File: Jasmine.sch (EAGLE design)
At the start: 26 parts, among them J4 GND, J6 Vcc, U1 ESP-12F, U3 XC6206

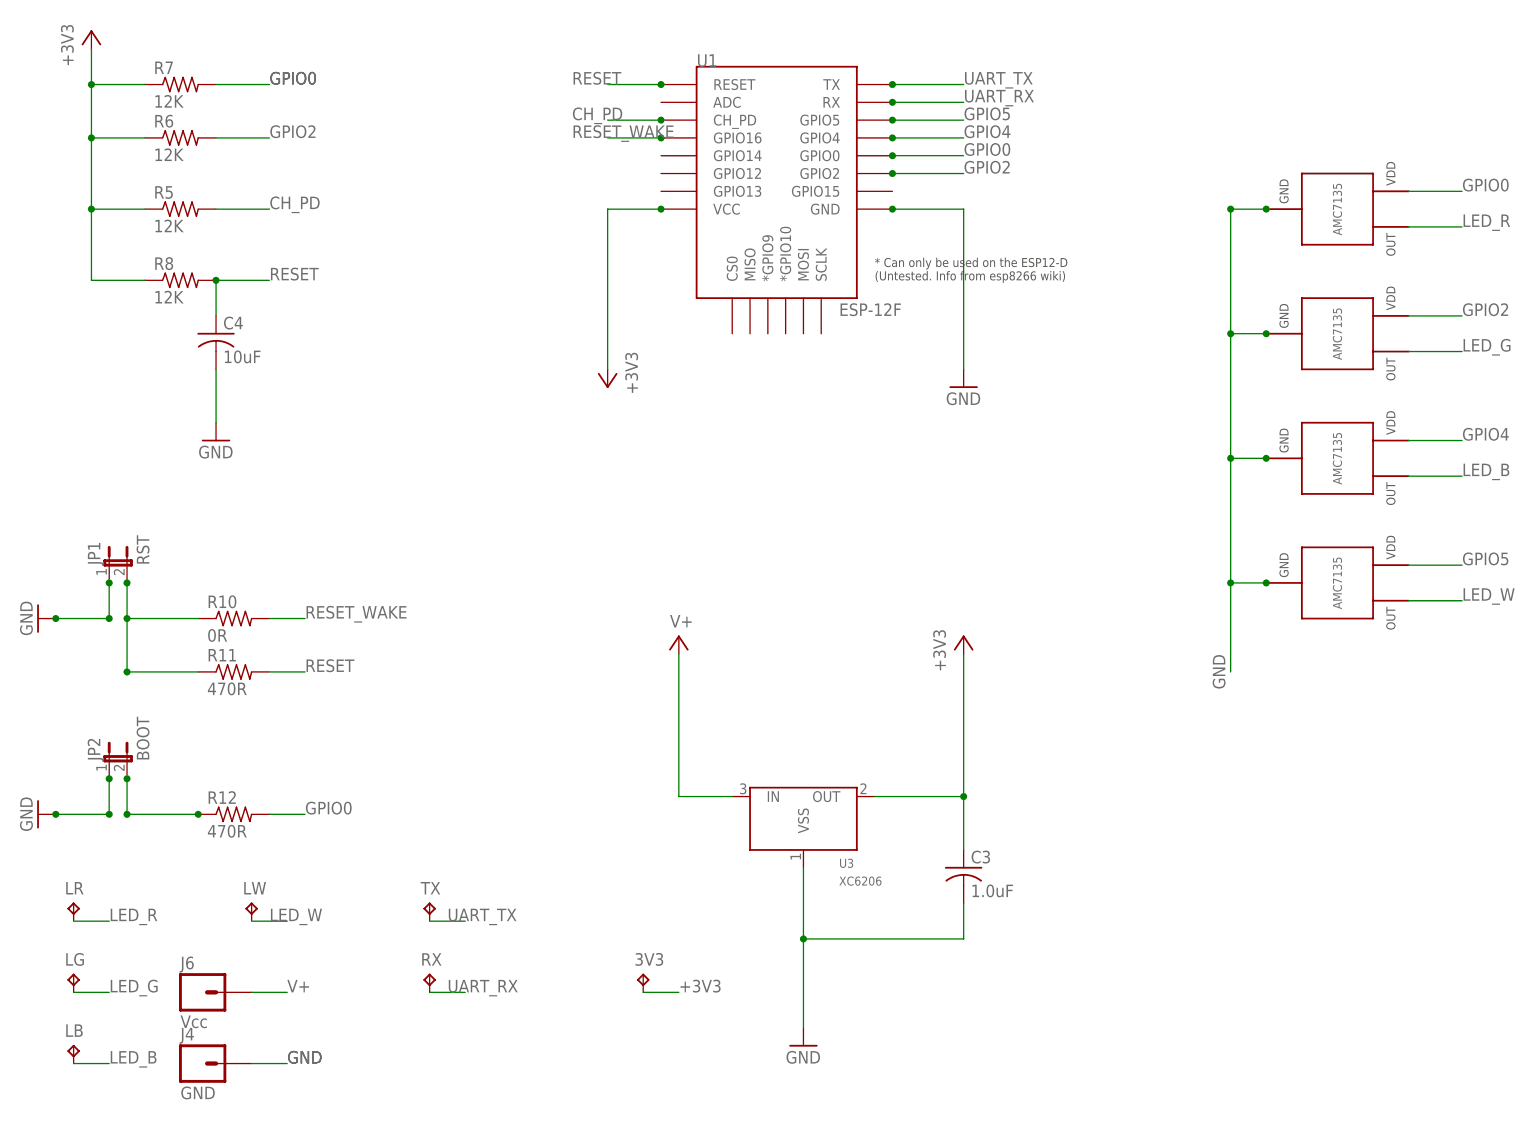
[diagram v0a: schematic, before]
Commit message: Add a software (factory) reset jumper
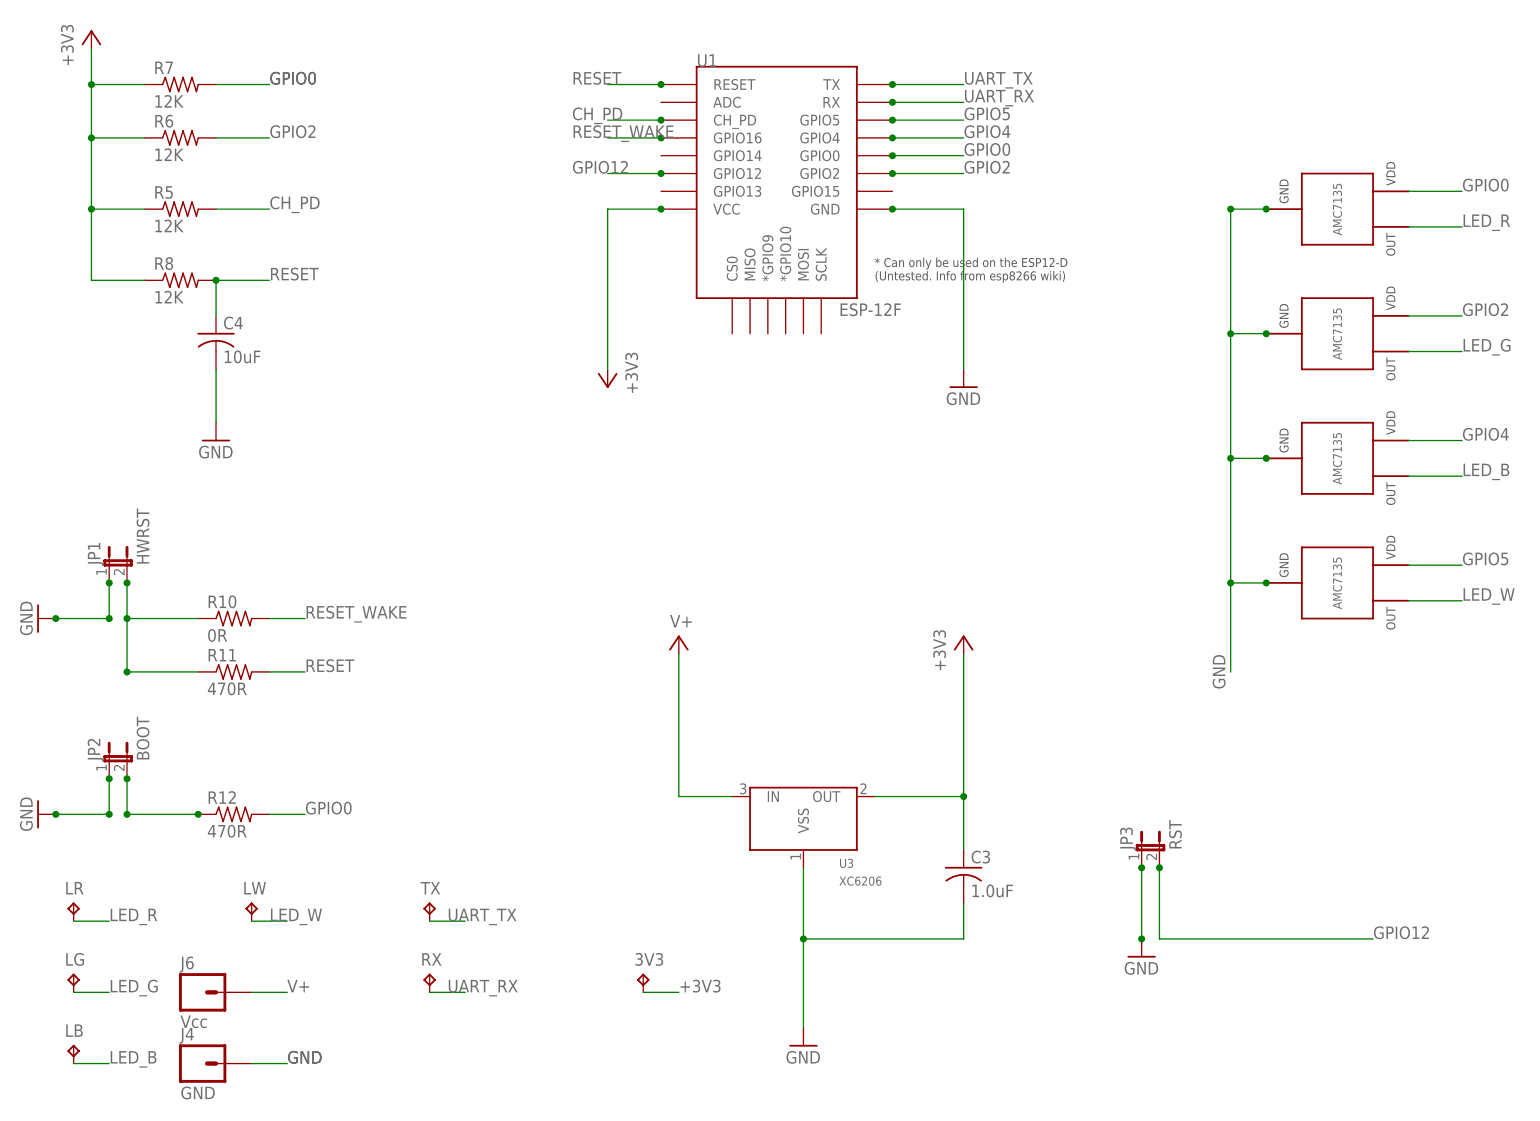
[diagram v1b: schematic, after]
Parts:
- added JP3: RST, SparkFun-Retired:JUMPER-2SMD-NO
- JP1: value RST -> HWRST
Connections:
- new net GPIO12: JP3.2, U1.GPIO12
- net GND: now also JP3.1
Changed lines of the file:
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@@
 <part name="RX" library="testpad" deviceset="TP" device="B2,54"/>
 <part name="3V3" library="testpad" deviceset="TP" device="B2,54"/>
-<part name="JP1" library="SparkFun-Retired" deviceset="JUMPER-2" device="SMD-NO" value="RST"/>
+<part name="JP1" library="SparkFun-Retired" deviceset="JUMPER-2" device="SMD-NO" value="HWRST"/>
 <part name="JP2" library="SparkFun-Retired" deviceset="JUMPER-2" device="SMD-NO" value="BOOT"/>
+<part name="JP3" library="SparkFun-Retired" deviceset="JUMPER-2" device="SMD-NO" value="RST"/>
+<part name="GND1" library="supply1" deviceset="GND" device=""/>
 </parts>
 <sheets>
@@
 <instance part="JP1" gate="A" x="-154.94" y="33.02"/>
 <instance part="JP2" gate="A" x="-154.94" y="5.08"/>
+<instance part="JP3" gate="A" x="-7.62" y="-7.62"/>
+<instance part="GND1" gate="1" x="-7.62" y="-22.86"/>
 </instances>
 <busses>
@@
 <pinref part="JP2" gate="A" pin="1"/>
 </segment>
+<segment>
+<pinref part="JP3" gate="A" pin="1"/>
+<wire x1="-7.62" y1="-10.16" x2="-7.62" y2="-20.32" width="0.1524" layer="91"/>
+<pinref part="GND1" gate="1" pin="GND"/>
+<junction x="-7.62" y="-10.16"/>
+<junction x="-7.62" y="-20.32"/>
+</segment>
 </net>
 <net name="+3V3" class="0">
@@
 </segment>
 </net>
+<net name="GPIO12" class="0">
+<segment>
+<pinref part="JP3" gate="A" pin="2"/>
+<wire x1="-5.08" y1="-10.16" x2="-5.08" y2="-20.32" width="0.1524" layer="91"/>
+<wire x1="-5.08" y1="-20.32" x2="25.4" y2="-20.32" width="0.1524" layer="91"/>
+<label x="25.4" y="-20.32" size="1.778" layer="95"/>
+<junction x="-5.08" y="-10.16"/>
+</segment>
+<segment>
+<pinref part="U1" gate="G$1" pin="GPIO12"/>
+<wire x1="-76.2" y1="88.9" x2="-83.82" y2="88.9" width="0.1524" layer="91"/>
+<label x="-88.9" y="88.9" size="1.778" layer="95"/>
+<junction x="-76.2" y="88.9"/>
+</segment>
+</net>
